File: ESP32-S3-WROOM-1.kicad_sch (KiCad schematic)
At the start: 24 parts, among them J11 Conn_01x08, J13 Conn_02x09_Top_Bottom, J14 Conn_01x09, J15 Conn_02x09_Top_Bottom, J4 JST-XH, J6 Conn_01x09, J7 Conn_02x20_Counter_Clockwise, J8 Conn_01x08, J9 Conn_01x08, SW4 SW_Push, U8 ESP32-S3-WROOM-1-N8R2

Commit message: Progress
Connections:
- net ESP_CS2: no longer U8.23 (GPIO21)
- net GPIO35: no longer J14.8 (Pin_8)
- net GPIO36: no longer J14.7 (Pin_7)
- net GPIO37: now also J14.9 (Pin_9); no longer J14.6 (Pin_6)
- net GPIO38: now also J14.8 (Pin_8); no longer J14.5 (Pin_5)
- net GPIO39: now also J14.7 (Pin_7); no longer J14.4 (Pin_4)
- net GPIO40: now also J14.6 (Pin_6); no longer J14.3 (Pin_3)
- net GPIO41: now also J14.5 (Pin_5); no longer J14.2 (Pin_2)
- net GPIO42: now also J14.4 (Pin_4); no longer J14.1 (Pin_1)
- net GPIO45: no longer J14.9 (Pin_9), U8.26 (GPIO45)
- net Pico_SCL1: now also J4.3, R21.2, U8.23 (GPIO21); no longer U8.37 (U0TXD/GPIO43/CLK_OUT1)
- net Pico_SDA1: now also J4.2, R20.2, U8.24 (GPIO47/SPICLK_P/SUBSPICLK_P_DIFF); no longer U8.36 (U0RXD/GPIO44/CLK_OUT2)
- net GPIO_2: now reaches U8.38 (GPIO2/TOUCH2/ADC1_CH1)
- net GPIO_2: now also J14.1 (Pin_1)
- removed net SCL: J4.3, J7.28 (Pin_28), R21.2, U8.25 (GPIO48/SPICLK_N/SUBSPICLK_N_DIFF)
- removed net SDA: J4.2, J7.27 (Pin_27), R20.2, U8.24 (GPIO47/SPICLK_P/SUBSPICLK_P_DIFF)
- new net GPIO_43: J14.2 (Pin_2), U8.37 (U0TXD/GPIO43/CLK_OUT1)
- new net GPIO_44: J14.3 (Pin_3), U8.36 (U0RXD/GPIO44/CLK_OUT2)
- new net TWI_SCL: J7.28 (Pin_28), U8.26 (GPIO45)
- new net TWI_SDA: J7.27 (Pin_27), U8.25 (GPIO48/SPICLK_N/SUBSPICLK_N_DIFF)
- no-connect marks 37 -> 35
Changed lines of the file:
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@@
-	)
-	(no_connect
-		(at 241.3 59.69)
 	)
 	(no_connect
@@
 	(no_connect
 		(at 33.02 110.49)
-	)
-	(no_connect
-		(at 248.92 97.79)
 	)
 	(no_connect
@@
 	(wire
 		(pts
-			(xy 248.92 102.87) (xy 241.3 102.87)
+			(xy 260.35 102.87) (xy 241.3 102.87)
 		)
 		(stroke
@@
 	(wire
 		(pts
+			(xy 241.3 59.69) (xy 248.92 59.69)
+		)
+		(stroke
+			(width 0)
+			(type default)
+		)
+	)
+	(wire
+		(pts
 			(xy 204.47 31.75) (xy 213.36 31.75)
 		)
@@
 	(wire
 		(pts
+			(xy 259.08 107.95) (xy 241.3 107.95)
+		)
+		(stroke
+			(width 0)
+			(type default)
+		)
+	)
+	(wire
+		(pts
 			(xy 85.09 57.15) (xy 87.63 57.15)
 		)
@@
 		)
 	)
-	(wire
-		(pts
-			(xy 248.92 97.79) (xy 241.3 97.79)
-		)
-		(stroke
-			(width 0)
-			(type default)
-		)
-	)
 	(polyline
 		(pts
@@
 	(wire
 		(pts
+			(xy 260.35 110.49) (xy 241.3 110.49)
+		)
+		(stroke
+			(width 0)
+			(type default)
+		)
+	)
+	(wire
+		(pts
 			(xy 85.09 62.23) (xy 87.63 62.23)
 		)
@@
 	(wire
 		(pts
+			(xy 259.08 106.68) (xy 259.08 107.95)
+		)
+		(stroke
+			(width 0)
+			(type default)
+		)
+	)
+	(wire
+		(pts
 			(xy 137.16 179.07) (xy 139.7 179.07)
 		)
@@
 	(wire
 		(pts
-			(xy 241.3 110.49) (xy 260.35 110.49)
+			(xy 241.3 97.79) (xy 260.35 97.79)
 		)
 		(stroke
@@
 	(wire
 		(pts
-			(xy 241.3 107.95) (xy 260.35 107.95)
+			(xy 259.08 106.68) (xy 260.35 106.68)
 		)
 		(stroke
@@
 		)
 	)
-	(label "TWI_SCL"
-		(at 260.35 110.49 0)
-		(fields_autoplaced yes)
-		(effects
-			(font
-				(size 1.27 1.27)
-			)
-			(justify left bottom)
+	(label "GPIO_44"
+		(at 85.09 52.07 180)
+		(fields_autoplaced yes)
+		(effects
+			(font
+				(size 1.27 1.27)
+			)
+			(justify right bottom)
 		)
 	)
@@
 		)
 	)
+	(label "GPIO39"
+		(at 85.09 62.23 180)
+		(fields_autoplaced yes)
+		(effects
+			(font
+				(size 1.27 1.27)
+			)
+			(justify right bottom)
+		)
+	)
 	(label "Handshake"
 		(at 59.69 176.53 0)
@@
 		)
 	)
-	(label "GPIO45"
-		(at 248.92 102.87 0)
-		(fields_autoplaced yes)
-		(effects
-			(font
-				(size 1.27 1.27)
-			)
-			(justify left bottom)
-		)
-	)
 	(label "USB_TX"
 		(at 78.74 137.16 0)
@@
 		)
 	)
-	(label "GPIO39"
-		(at 85.09 54.61 180)
-		(fields_autoplaced yes)
-		(effects
-			(font
-				(size 1.27 1.27)
-			)
-			(justify right bottom)
-		)
-	)
 	(label "GPIO37"
 		(at 146.05 110.49 180)
@@
 		)
 	)
+	(label "GPIO45"
+		(at 78.74 74.93 180)
+		(fields_autoplaced yes)
+		(effects
+			(font
+				(size 1.27 1.27)
+			)
+			(justify right bottom)
+		)
+	)
 	(label "GPIO_15"
 		(at 118.11 99.06 180)
@@
 	)
 	(label "ESP_CS2"
-		(at 248.92 97.79 0)
+		(at 273.05 102.87 0)
 		(fields_autoplaced yes)
 		(effects
@@
 		)
 	)
-	(label "GPIO45"
-		(at 85.09 67.31 180)
-		(fields_autoplaced yes)
-		(effects
-			(font
-				(size 1.27 1.27)
-			)
-			(justify right bottom)
-		)
-	)
-	(label "GPIO42"
-		(at 85.09 46.99 180)
-		(fields_autoplaced yes)
-		(effects
-			(font
-				(size 1.27 1.27)
-			)
-			(justify right bottom)
+	(label "TWI_SCL"
+		(at 260.35 102.87 0)
+		(fields_autoplaced yes)
+		(effects
+			(font
+				(size 1.27 1.27)
+			)
+			(justify left bottom)
 		)
 	)
@@
 		)
 	)
-	(label "GPIO35"
-		(at 85.09 64.77 180)
-		(fields_autoplaced yes)
-		(effects
-			(font
-				(size 1.27 1.27)
-			)
-			(justify right bottom)
-		)
-	)
 	(label "ESP_CS0"
 		(at 137.16 176.53 180)
@@
 		)
 	)
+	(label "GPIO_44"
+		(at 252.73 41.91 0)
+		(fields_autoplaced yes)
+		(effects
+			(font
+				(size 1.27 1.27)
+			)
+			(justify left bottom)
+		)
+	)
 	(label "GPIO40"
 		(at 143.51 57.15 180)
@@
 		)
 	)
+	(label "GPIO35"
+		(at 78.74 72.39 180)
+		(fields_autoplaced yes)
+		(effects
+			(font
+				(size 1.27 1.27)
+			)
+			(justify right bottom)
+		)
+	)
 	(label "ADC1"
 		(at 113.03 91.44 0)
@@
 	)
 	(label "SCL"
-		(at 250.19 110.49 0)
+		(at 248.92 97.79 0)
 		(fields_autoplaced yes)
 		(effects
@@
 		)
 	)
+	(label "GPIO36"
+		(at 78.74 69.85 180)
+		(fields_autoplaced yes)
+		(effects
+			(font
+				(size 1.27 1.27)
+			)
+			(justify right bottom)
+		)
+	)
 	(label "TWI_SCL"
 		(at 53.34 97.79 0)
@@
 		)
 	)
-	(label "GPIO37"
-		(at 85.09 59.69 180)
-		(fields_autoplaced yes)
-		(effects
-			(font
-				(size 1.27 1.27)
-			)
-			(justify right bottom)
-		)
-	)
 	(label "ADC3"
 		(at 241.3 72.39 0)
@@
 		)
 	)
-	(label "TWI_SDA"
-		(at 260.35 107.95 0)
-		(fields_autoplaced yes)
-		(effects
-			(font
-				(size 1.27 1.27)
-			)
-			(justify left bottom)
+	(label "GPIO40"
+		(at 85.09 59.69 180)
+		(fields_autoplaced yes)
+		(effects
+			(font
+				(size 1.27 1.27)
+			)
+			(justify right bottom)
+		)
+	)
+	(label "GPIO37"
+		(at 85.09 67.31 180)
+		(fields_autoplaced yes)
+		(effects
+			(font
+				(size 1.27 1.27)
+			)
+			(justify right bottom)
 		)
 	)
@@
 		)
 	)
+	(label "TWI_SDA"
+		(at 260.35 110.49 0)
+		(fields_autoplaced yes)
+		(effects
+			(font
+				(size 1.27 1.27)
+			)
+			(justify left bottom)
+		)
+	)
+	(label "GPIO_2"
+		(at 85.09 46.99 180)
+		(fields_autoplaced yes)
+		(effects
+			(font
+				(size 1.27 1.27)
+			)
+			(justify right bottom)
+		)
+	)
 	(label "GPIO_17"
 		(at 118.11 104.14 180)
@@
 		)
 	)
-	(label "GPIO36"
-		(at 85.09 62.23 180)
-		(fields_autoplaced yes)
-		(effects
-			(font
-				(size 1.27 1.27)
-			)
-			(justify right bottom)
+	(label "GPIO_2"
+		(at 248.92 59.69 0)
+		(fields_autoplaced yes)
+		(effects
+			(font
+				(size 1.27 1.27)
+			)
+			(justify left bottom)
 		)
 	)
@@
 		)
 	)
+	(label "GPIO_43"
+		(at 252.73 39.37 0)
+		(fields_autoplaced yes)
+		(effects
+			(font
+				(size 1.27 1.27)
+			)
+			(justify left bottom)
+		)
+	)
 	(label "Handshake2"
 		(at 248.92 90.17 0)
@@
 		)
 	)
-	(label "GPIO41"
-		(at 85.09 49.53 180)
-		(fields_autoplaced yes)
-		(effects
-			(font
-				(size 1.27 1.27)
-			)
-			(justify right bottom)
-		)
-	)
 	(label "GPIO38"
-		(at 85.09 57.15 180)
+		(at 85.09 64.77 180)
 		(fields_autoplaced yes)
 		(effects
@@
 		)
 	)
-	(label "GPIO40"
-		(at 85.09 52.07 180)
+	(label "GPIO_43"
+		(at 85.09 49.53 180)
+		(fields_autoplaced yes)
+		(effects
+			(font
+				(size 1.27 1.27)
+			)
+			(justify right bottom)
+		)
+	)
+	(label "GPIO42"
+		(at 85.09 54.61 180)
+		(fields_autoplaced yes)
+		(effects
+			(font
+				(size 1.27 1.27)
+			)
+			(justify right bottom)
+		)
+	)
+	(label "GPIO41"
+		(at 85.09 57.15 180)
 		(fields_autoplaced yes)
 		(effects
@@
 		)
 	)
-	(global_label "Pico_SDA1"
+	(global_label "Pico_SCL1"
 		(shape input)
-		(at 252.73 41.91 0)
+		(at 260.35 97.79 0)
 		(fields_autoplaced yes)
 		(effects
@@
 		)
 		(property "Intersheetrefs" "${INTERSHEET_REFS}"
-			(at 265.5728 41.91 0)
+			(at 273.1323 97.79 0)
 			(effects
 				(font
@@
 		)
 	)
-	(global_label "Pico_SCL1"
+	(global_label "Pico_SDA1"
 		(shape input)
-		(at 252.73 39.37 0)
+		(at 260.35 106.68 0)
 		(fields_autoplaced yes)
 		(effects
@@
 		)
 		(property "Intersheetrefs" "${INTERSHEET_REFS}"
-			(at 265.5123 39.37 0)
+			(at 273.1928 106.68 0)
 			(effects
 				(font

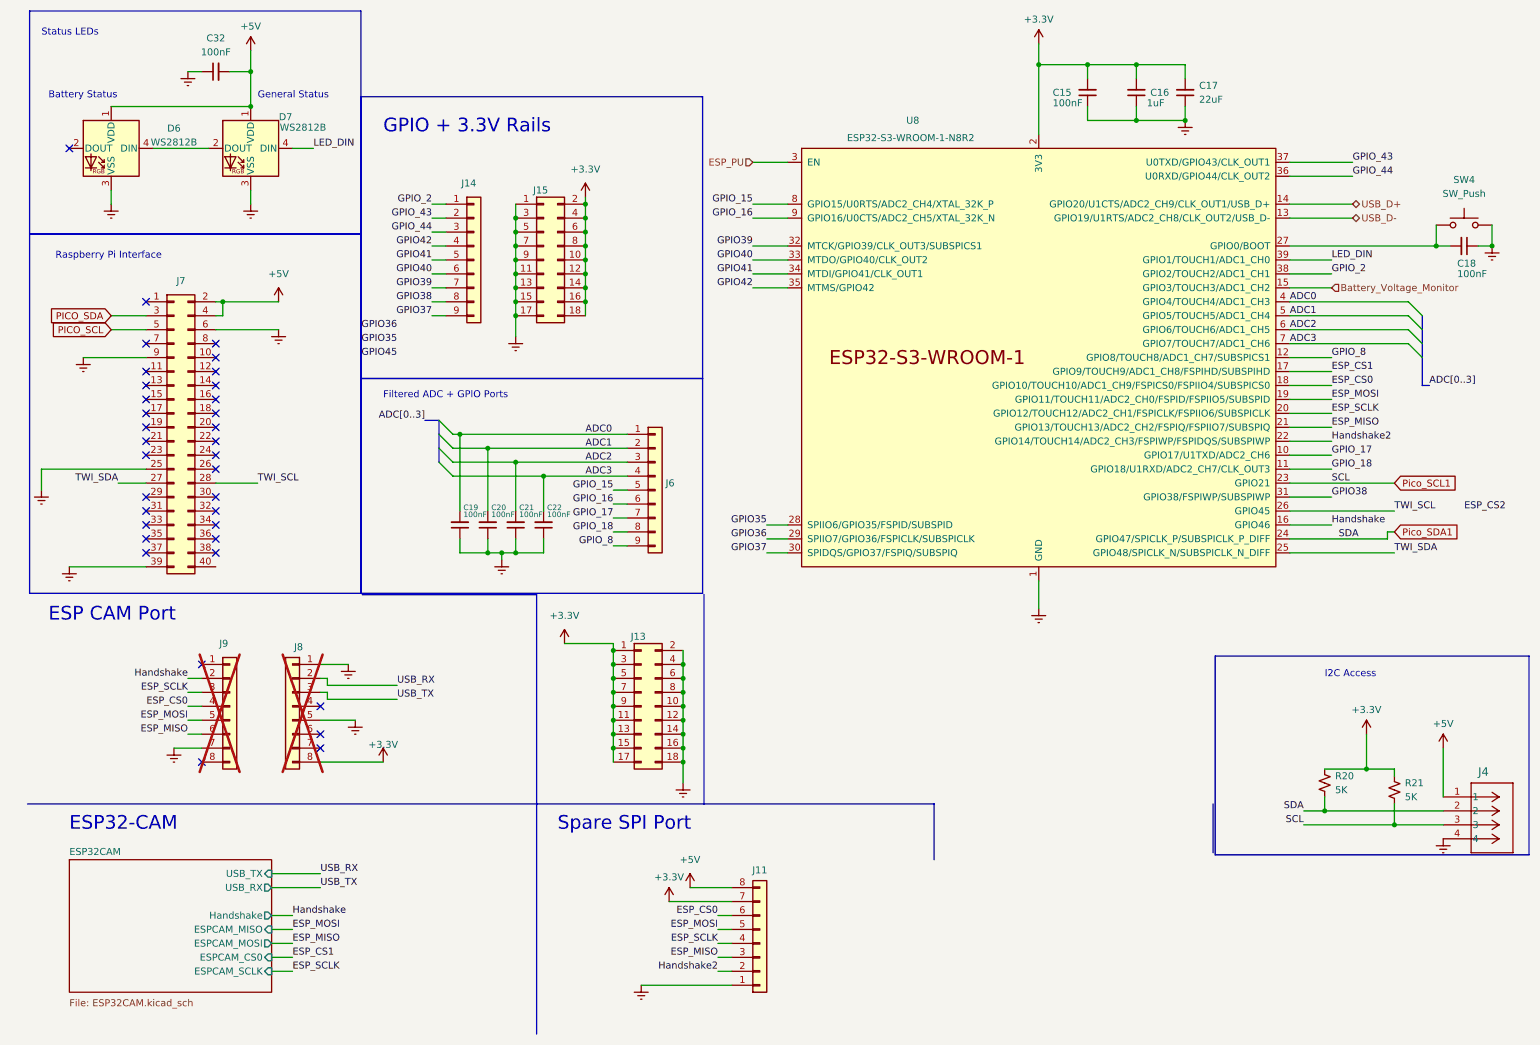
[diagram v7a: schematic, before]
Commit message: Layout for 80x80mm done
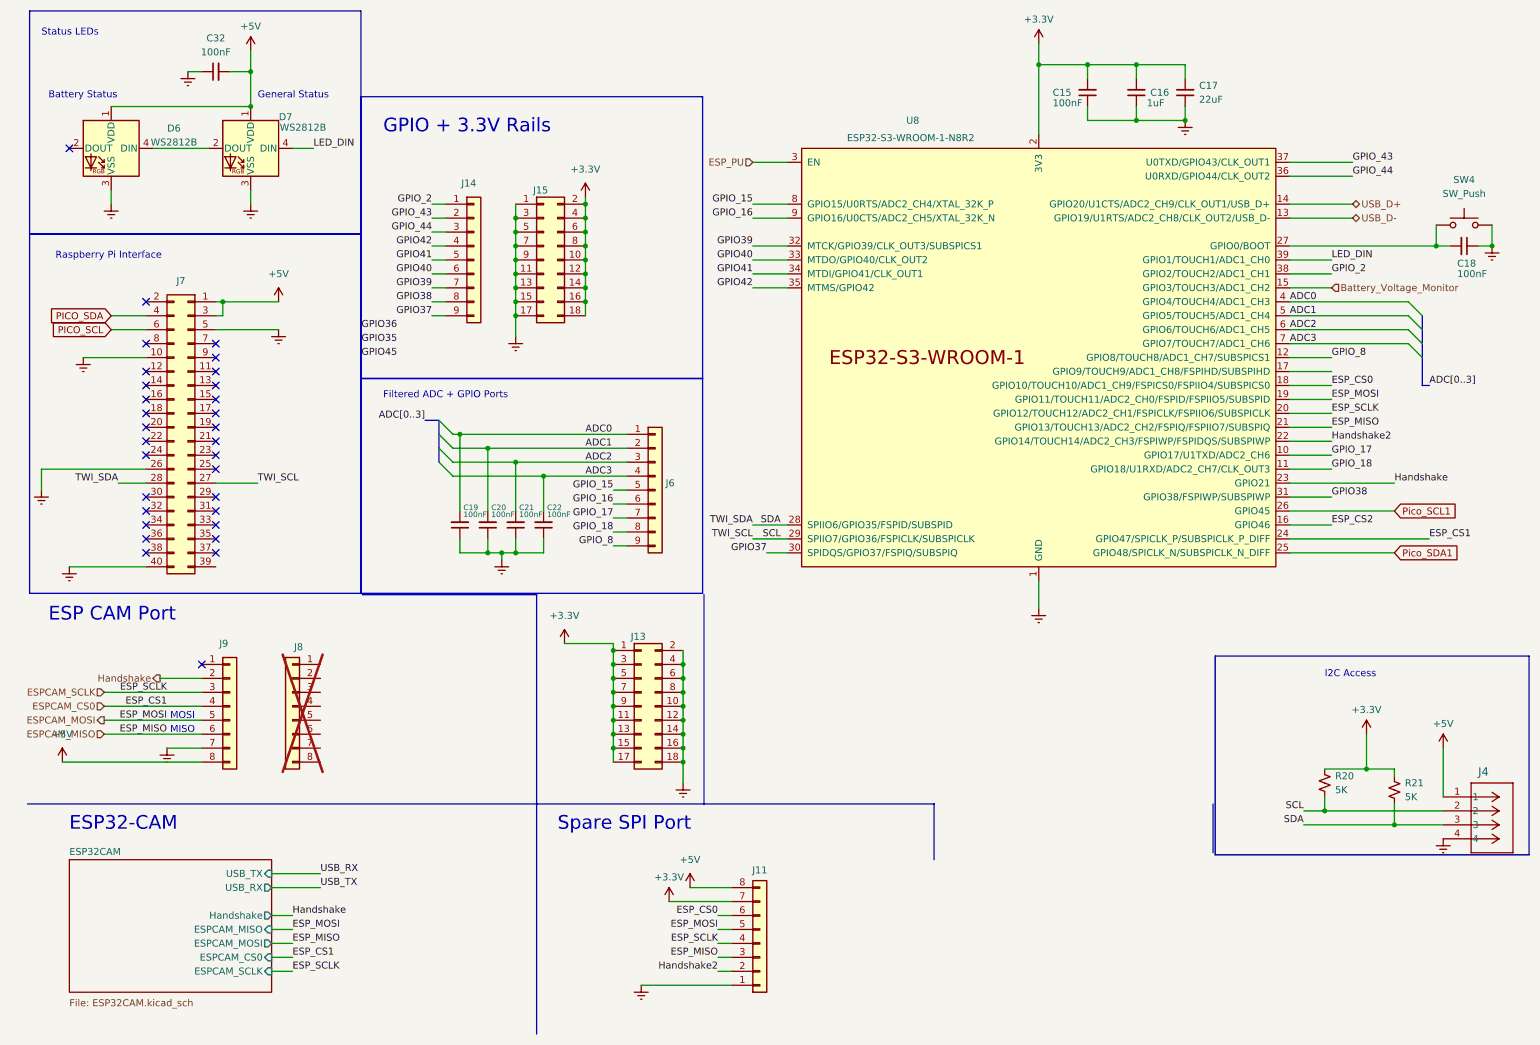
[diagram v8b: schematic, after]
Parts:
- J9: now fitted
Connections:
- net +3.3V: no longer J8.8 (Pin_8)
- net +5V: now also J7.1 (Pin_1), J7.3 (Pin_3), J9.8 (Pin_8); no longer J7.2 (Pin_2), J7.4 (Pin_4)
- net ESP_CS0: no longer J9.4 (Pin_4)
- net ESP_CS2: now also U8.16 (GPIO46)
- net Earth: now also J7.10 (Pin_10), J7.26 (Pin_26), J7.40 (Pin_40), J7.5 (Pin_5); no longer J7.25 (Pin_25), J7.39 (Pin_39), J7.6 (Pin_6), J7.9 (Pin_9), J8.1 (Pin_1), J8.5 (Pin_5)
- net GPIO35: no longer U8.28 (SPIIO6/GPIO35/FSPID/SUBSPID)
- net GPIO36: no longer U8.29 (SPIIO7/GPIO36/FSPICLK/SUBSPICLK)
- net Handshake: now also U8.23 (GPIO21); no longer U8.16 (GPIO46)
- net PICO_SCL: now also J7.6 (Pin_6); no longer J7.5 (Pin_5)
- net PICO_SDA: now also J7.4 (Pin_4); no longer J7.3 (Pin_3)
- net Pico_SCL1: now also U8.26 (GPIO45); no longer J4.3, R21.2, U8.23 (GPIO21)
- net Pico_SDA1: now also U8.25 (GPIO48/SPICLK_N/SUBSPICLK_N_DIFF); no longer J4.2, R20.2, U8.24 (GPIO47/SPICLK_P/SUBSPICLK_P_DIFF)
- net USB_RX: no longer J8.2 (Pin_2)
- net USB_TX: no longer J8.3 (Pin_3)
- net ESP_CS1: no longer names the net of U8.17 (GPIO9/TOUCH9/ADC1_CH8/FSPIHD/SUBSPIHD)
- net ESP_MISO renamed ESPCAM_MISO
- net ESP_MOSI renamed ESPCAM_MOSI
- net ESP_SCLK renamed ESPCAM_SCLK
- net TWI_SCL renamed SDA
- net SDA: now also J4.3, R21.2, U8.28 (SPIIO6/GPIO35/FSPID/SUBSPID); no longer U8.26 (GPIO45)
- net TWI_SDA renamed SCL
- net SCL: now also J4.2, R20.2, U8.29 (SPIIO7/GPIO36/FSPICLK/SUBSPICLK); no longer U8.25 (GPIO48/SPICLK_N/SUBSPICLK_N_DIFF)
- new net ESPCAM_CS0: J9.4 (Pin_4), U8.24 (GPIO47/SPICLK_P/SUBSPICLK_P_DIFF)
- no-connect marks 35 -> 31
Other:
- note added: "MISO"
- note added: "MOSI"
